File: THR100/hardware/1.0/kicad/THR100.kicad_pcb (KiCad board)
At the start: 2 copper layers, 75 x 75 mm, 51 parts, among them J1 CAN, J2 SWITCHES, J3 ANALOG_IN, J4 Screw_Terminal_01x02, J5 Screw_Terminal_01x02, K1 FINDER-32.21-x300, K2 FINDER-32.21-x300, Q1 NTE123A, Q2 NTE123A, SW1 MISC, SW2 MODE, SW3 INSTANCE, U1 MCP2551-I-P, U2 TMR-1-1211, U3 Teensy_3.2, U4 CNY74-2H

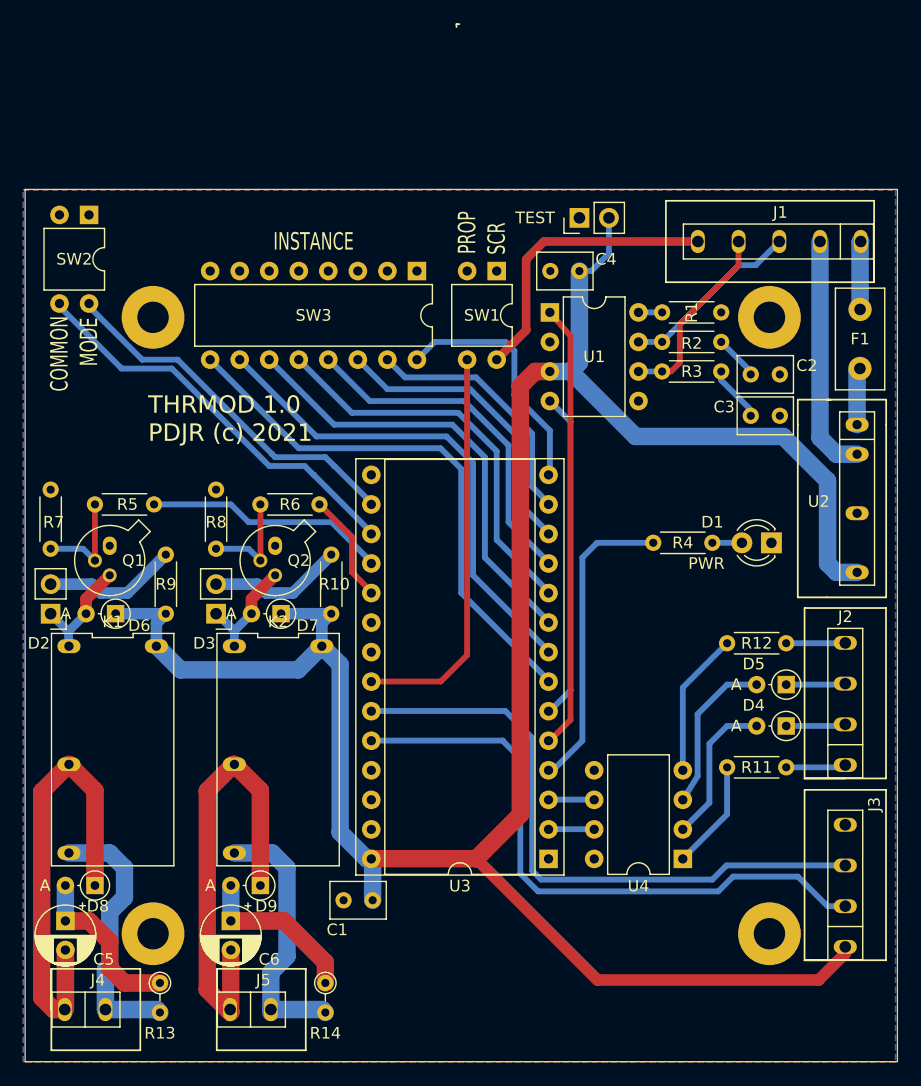
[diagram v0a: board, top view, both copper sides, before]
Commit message: Add azimuth support
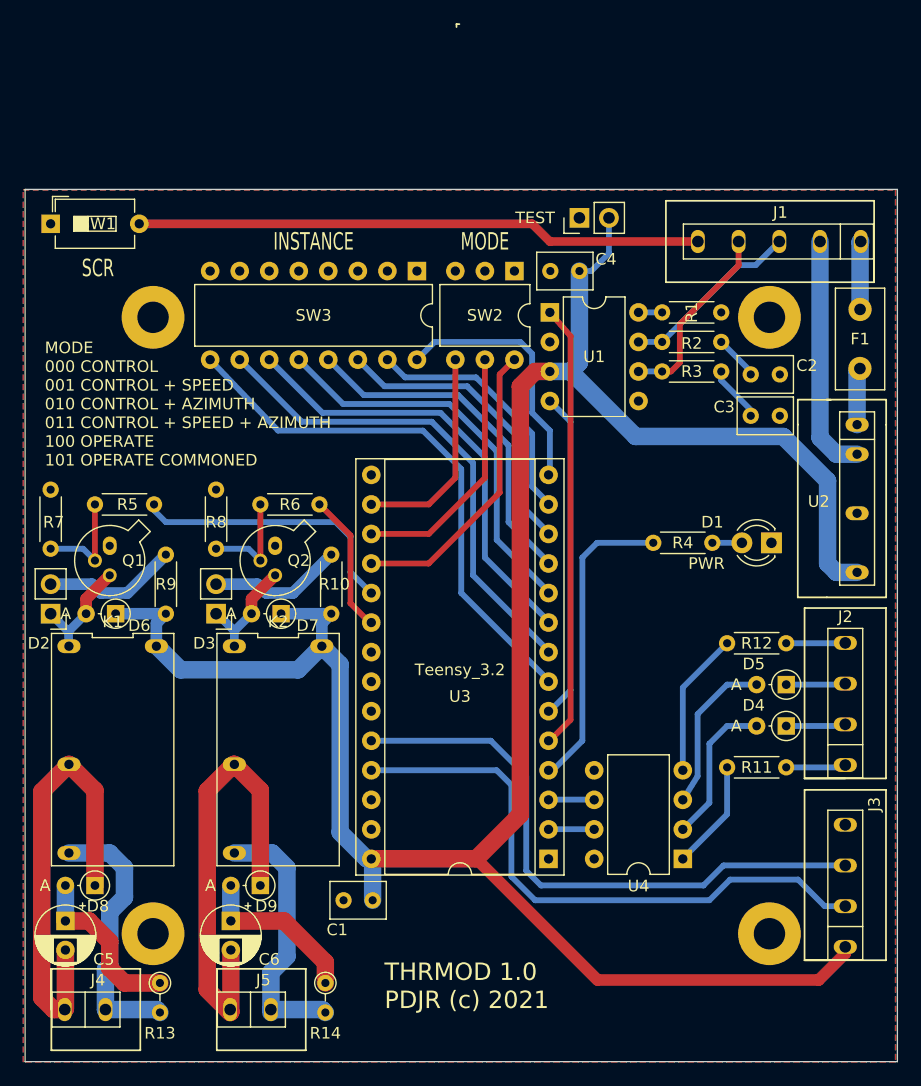
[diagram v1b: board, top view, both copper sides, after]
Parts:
- SW1: value MISC -> SCR; footprint Package_DIP:DIP-4_W7.62mm -> Button_Switch_THT:SW_DIP_SPSTx01_Slide_6.7x4.1mm_W7.62mm_P2.54mm_LowProfile
- SW2: footprint Package_DIP:DIP-4_W7.62mm -> Package_DIP:DIP-6_W7.62mm
- moved SW1 38.6 mm to (138.4, 89.9), turned to 0 degrees
- moved SW2 36.9 mm to (178.2, 94.0)
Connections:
- net /MODE_SEL renamed /MODE_ADDR_2
- J3 pad 2: /SB_ADC -> /SPEED
- J3 pad 3: /PS_ADC -> /AZIMUTH
- SW1 pad 2: GND -> /CAN_SCR
- SW2 pad 3: /COMMON -> GND
- U3 pad 17: /COMMON -> /MODE_ADDR_1
- U3 pad 18: /PS_RLY -> /MODE_ADDR_0
- U3 pad 19: /SB_RLY -> /PS_RLY
- U3 pad 20: (no net) -> /SB_RLY
- U3 pad 22: /ANALOG -> (no net)
- U3 pad 23: /PS_ADC -> (no net)
- U3 pad 24: /SB_ADC -> /AZIMUTH
- U3 pad 25: (no net) -> /SPEED
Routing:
- net /PS_ADC: track 53.8 -> 0.00 mm
- net /SB_ADC: track 53.4 -> 0.00 mm
- net /SPEED: track 0.00 -> 51.7 mm
- net /AZIMUTH: track 0.00 -> 51.4 mm
- net /COMMON: track 35.0 -> 0.00 mm
- net /ANALOG: track 34.5 -> 0.00 mm
- net /MODE_ADDR_0: track 0.00 -> 25.5 mm
- net /CAN_SCR: track 25.1 -> 48.7 mm
- net /MODE_ADDR_1: track 0.00 -> 21.9 mm
- net /MODE_ADDR_2: track 31.4 -> 18.3 mm
- net /PS_RLY: track 20.9 -> 23.9 mm
- net /SB_RLY: track 9.50 -> 12.1 mm
- net /ADDR_0: track 21.6 -> 22.3 mm
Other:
- board text added: "MODE 000 CONTROL 001 CONTROL + SPEED 010 CONTROL + AZIMUTH 011 CONTROL + SPEED + AZIMUTH 100 OPERATE 101 OPERATE COMMONED"
- board text removed: "COMMON"
- board text removed: "MODE"
- board text removed: "PROP"
- board text removed: "SCR"
